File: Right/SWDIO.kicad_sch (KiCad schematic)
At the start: 1 part

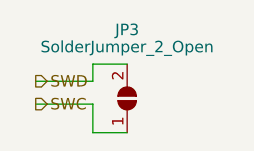
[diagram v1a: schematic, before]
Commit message: upgraded files to kicad7
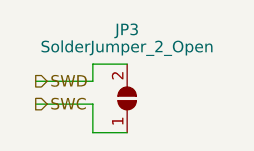
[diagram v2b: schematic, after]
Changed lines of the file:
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@@
-(kicad_sch (version 20211123) (generator eeschema)
+(kicad_sch (version 20230121) (generator eeschema)
   (paper "A4")
   (wire (pts (xy 128.905 104.14) (xy 135.255 104.14))
-    (stroke (width 0) (type default) (color 0 0 0 0))
+    (stroke (width 0) (type default))
   )
   (wire (pts (xy 135.255 106.68) (xy 135.255 109.855))
-    (stroke (width 0) (type default) (color 0 0 0 0))
+    (stroke (width 0) (type default))
   )
   (wire (pts (xy 135.255 104.14) (xy 135.255 102.235))
-    (stroke (width 0) (type default) (color 0 0 0 0))
+    (stroke (width 0) (type default))
   )
   (wire (pts (xy 135.255 102.235) (xy 139.065 102.235))
-    (stroke (width 0) (type default) (color 0 0 0 0))
+    (stroke (width 0) (type default))
   )
   (wire (pts (xy 135.255 109.855) (xy 139.065 109.855))
-    (stroke (width 0) (type default) (color 0 0 0 0))
+    (stroke (width 0) (type default))
   )
   (wire (pts (xy 128.905 106.68) (xy 135.255 106.68))
-    (stroke (width 0) (type default) (color 0 0 0 0))
+    (stroke (width 0) (type default))
   )
-  (hierarchical_label "SWC" (shape output) (at 128.905 106.68 0)
+  (hierarchical_label "SWC" (shape output) (at 128.905 106.68 0) (fields_autoplaced)
     (effects (font (size 1.27 1.27)) (justify left))
   )
-  (hierarchical_label "SWD" (shape output) (at 128.905 104.14 0)
+  (hierarchical_label "SWD" (shape output) (at 128.905 104.14 0) (fields_autoplaced)
     (effects (font (size 1.27 1.27)) (justify left))
   )
   (symbol (lib_id "Jumper:SolderJumper_2_Open") (at 139.065 106.045 270) (mirror x) (unit 1)
-    (in_bom yes) (on_board yes)
-    (property "Reference" "JP3" (id 0) (at 139.065 98.425 90))
-    (property "Value" "SolderJumper_2_Open" (id 1) (at 139.065 100.33 90))
-    (property "Footprint" "Jumper:SolderJumper-2_P1.3mm_Open_RoundedPad1.0x1.5mm" (id 2) (at 139.065 106.045 0)
+    (in_bom yes) (on_board yes) (dnp no)
+    (property "Reference" "JP3" (at 139.065 98.425 90)
+      (effects (font (size 1.27 1.27)))
+    )
+    (property "Value" "SolderJumper_2_Open" (at 139.065 100.33 90)
+      (effects (font (size 1.27 1.27)))
+    )
+    (property "Footprint" "Jumper:SolderJumper-2_P1.3mm_Open_RoundedPad1.0x1.5mm" (at 139.065 106.045 0)
       (effects (font (size 1.27 1.27)) hide)
     )
-    (property "Datasheet" "~" (id 3) (at 139.065 106.045 0)
+    (property "Datasheet" "~" (at 139.065 106.045 0)
       (effects (font (size 1.27 1.27)) hide)
     )
     (pin "1")
     (pin "2")
+    (instances
+      (project "Right"
+        (path "/94899d91-c8b6-48a0-9eee-db2609092a2a/ff12d1ae-3ae9-40c8-917e-31f2acbc2f42"
+          (reference "JP3") (unit 1)
+        )
+      )
+    )
   )
 )
